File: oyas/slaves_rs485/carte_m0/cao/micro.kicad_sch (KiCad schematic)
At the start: 19 parts, among them J4 ISCP, U4 ATSAMD21G18A-A

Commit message: Finitions PCB
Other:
- company: (none) -> BPC
- title: (none) -> Carte Oya M0
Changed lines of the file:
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@@
 (kicad_sch (version 20230121) (generator eeschema)
   (paper "A4")
+  (title_block
+    (title "Carte Oya M0")
+    (date "2026-03-06")
+    (rev "Rev A")
+    (company "BPC")
+  )
   (junction (at 137.16 175.26) (diameter 0) (color 0 0 0 0)
   )

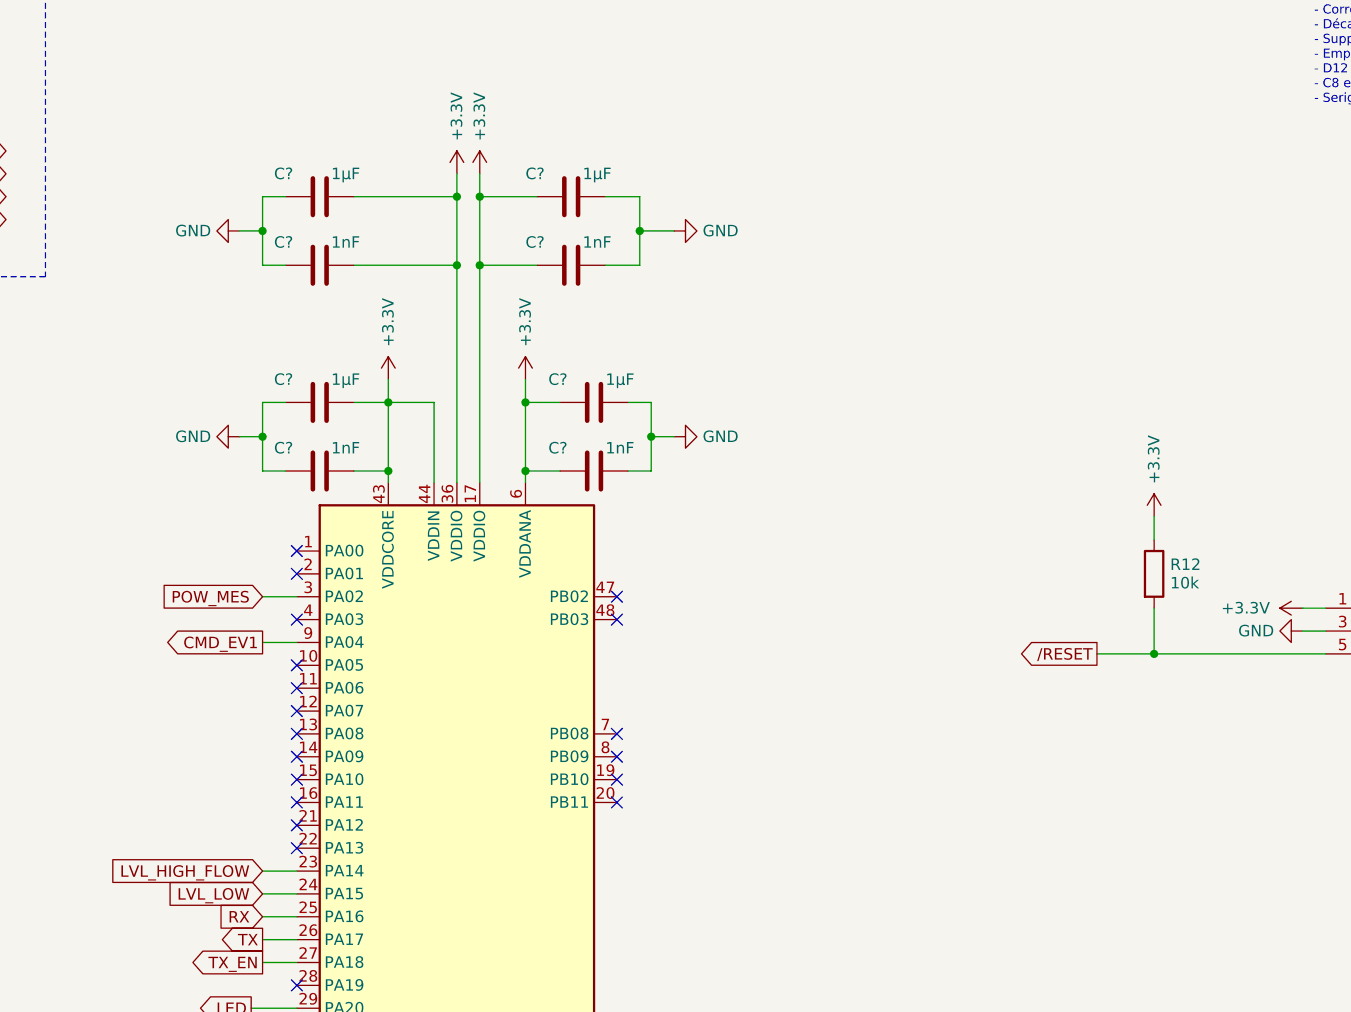
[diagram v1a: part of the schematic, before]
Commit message: Revue de carte et de routage:
- Amélioration découplage micro (1uF 805 sur VDDCore et 100nF 603 sur les autres selon recommendation microchip)
- R14=1k: Moins de courant dans Q1
- R1=R2=1k: Limiter le clamp en mode débit
- R3 NM en mode débit
- C17=100nF pour améliorer filtrage 3.3V
- Ajout Capa 100nF sur reset
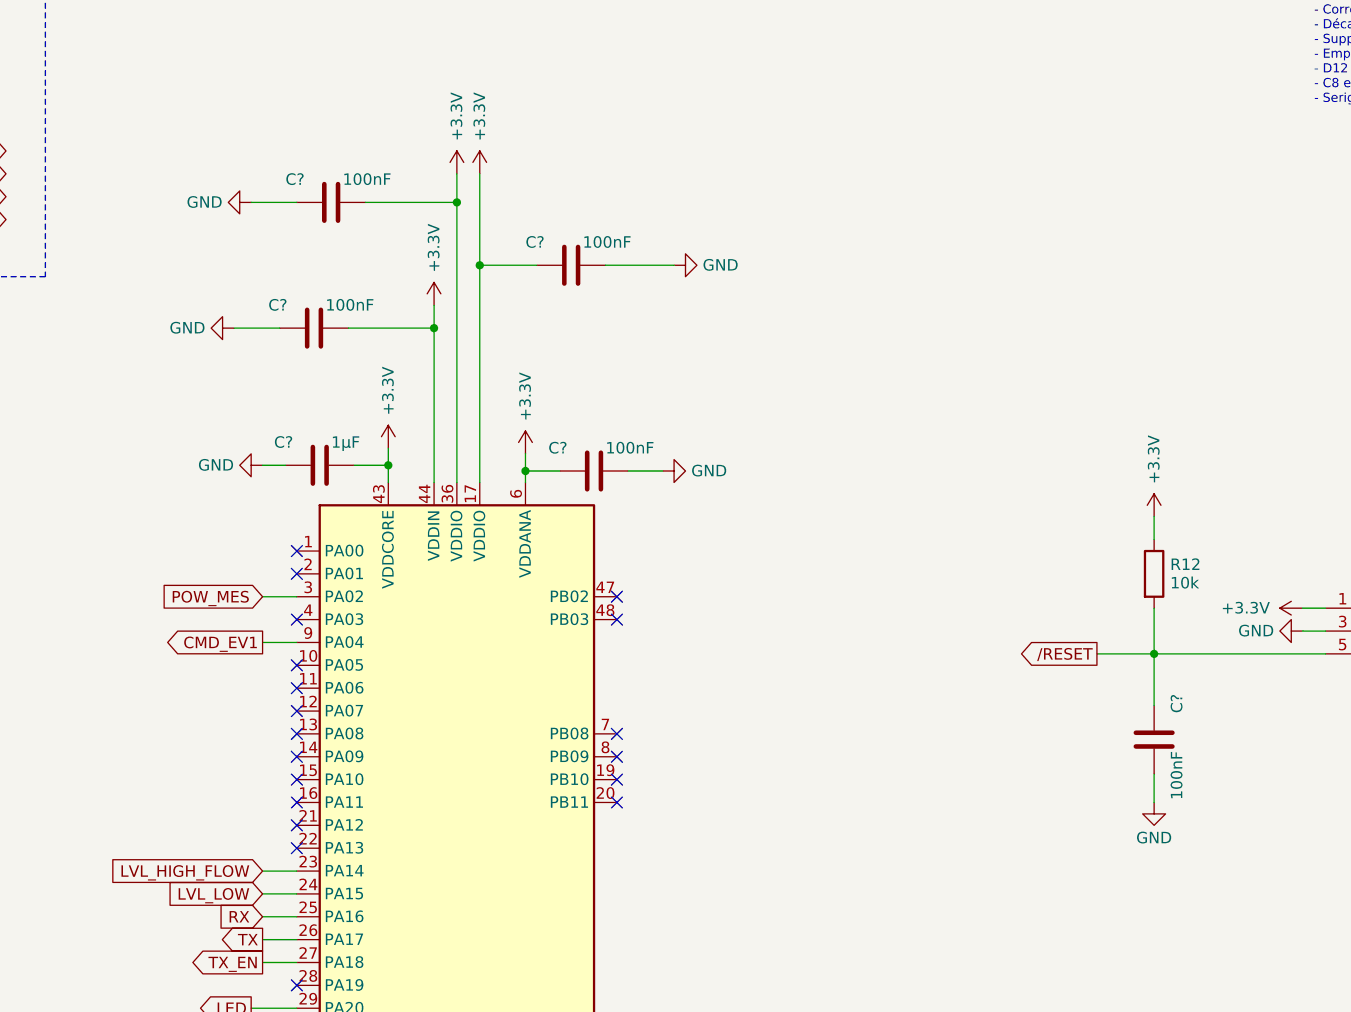
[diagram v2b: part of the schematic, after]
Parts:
- removed C? (x3): 1µF, Capacitor_SMD:C_0603_1608Metric_Pad1.08x0.95mm_HandSolder, symbol Device:C
- removed C?: 1nF, Capacitor_SMD:C_0603_1608Metric_Pad1.08x0.95mm_HandSolder, symbol Device:C
- added C?: 100nF, Capacitor_SMD:C_0603_1608Metric_Pad1.08x0.95mm_HandSolder, symbol Device:C
- added C?: 100nF, Capacitor_SMD:C_0805_2012Metric_Pad1.18x1.45mm_HandSolder, symbol Device:C
- C? (x3): value 1nF -> 100nF
- C?: footprint Capacitor_SMD:C_0603_1608Metric_Pad1.08x0.95mm_HandSolder -> Capacitor_SMD:C_0805_2012Metric_Pad1.18x1.45mm_HandSolder
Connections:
- net +3.3V: now also C?.1
- net GND: now also C?.1, C?.2
- net /RESET: now also C?.2
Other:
- moved on the sheet: C?

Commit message: Fin de revue avec ajout d'une diode TVS 18V en entrée
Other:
- title: Carte Oya M0 -> Esclave Oya M0
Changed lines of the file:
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@@
   (paper "A4")
   (title_block
-    (title "Carte Oya M0")
-    (date "2026-03-06")
-    (rev "Rev A")
+    (title "Esclave Oya M0")
+    (date "2026-03-07")
+    (rev "A")
     (company "BPC")
+    (comment 1 "Technologie avec M0 / Petite carte")
+    (comment 2 "Monitoring de tension d'alimentation")
+    (comment 3 "1 sortie 12V/5A - 2 entrées TOR (niveaux) ou 1 débimètre - 1 LED - RS485")
   )
   (junction (at 137.16 175.26) (diameter 0) (color 0 0 0 0)

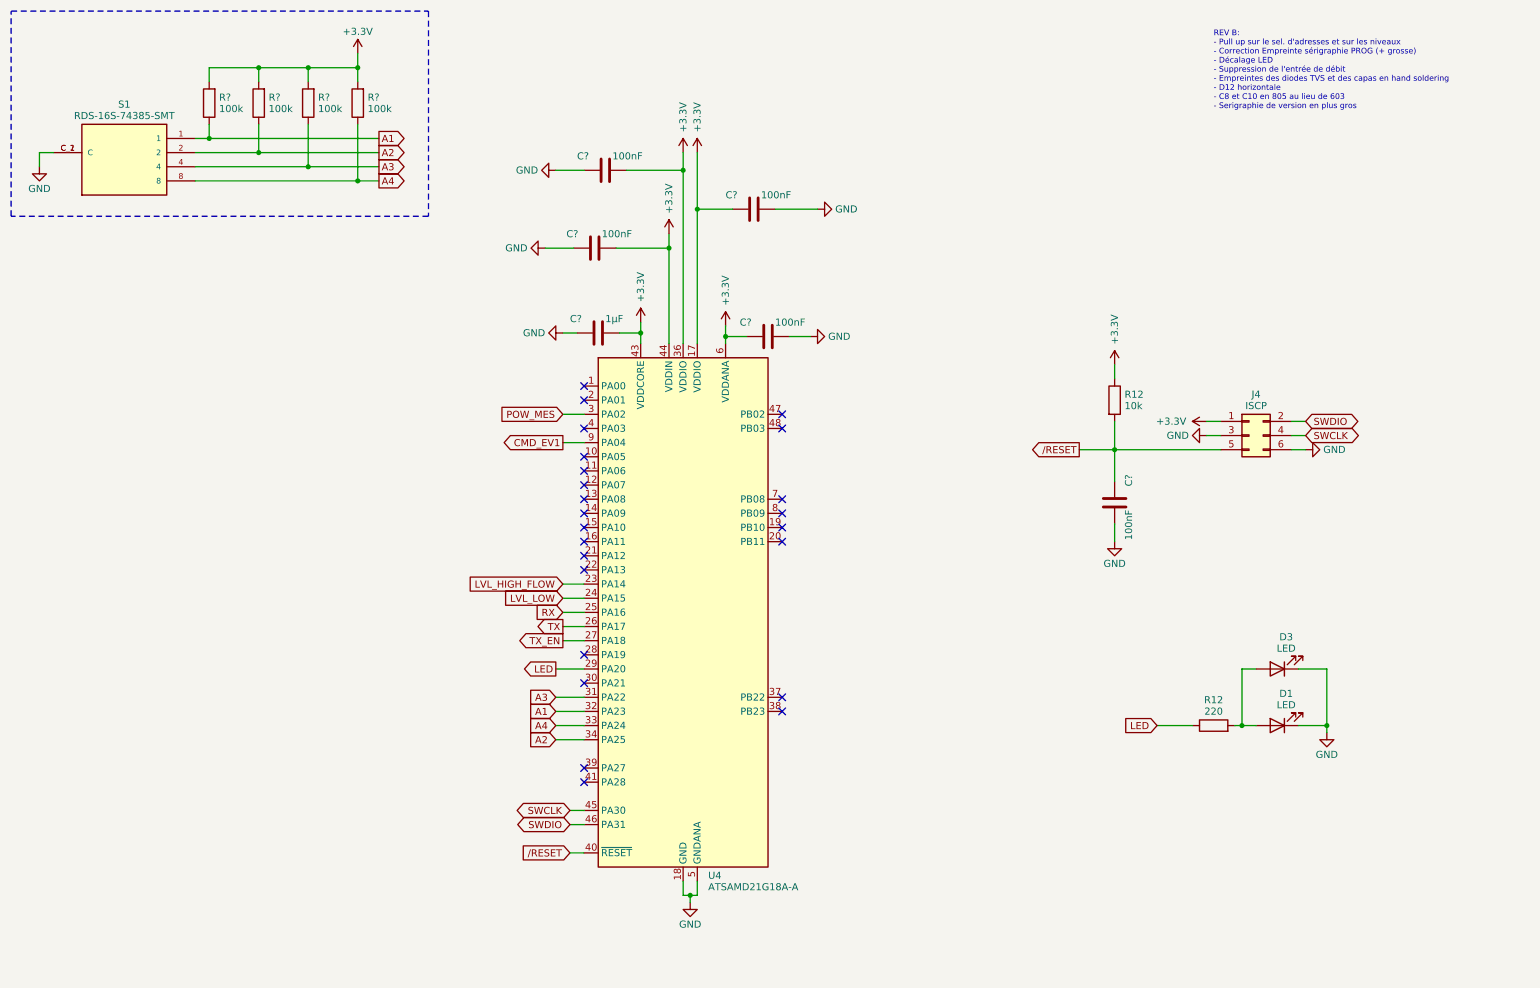
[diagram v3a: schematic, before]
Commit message: Préparation future carte Rev B (Inversion TX/RX) Programme en cours de test
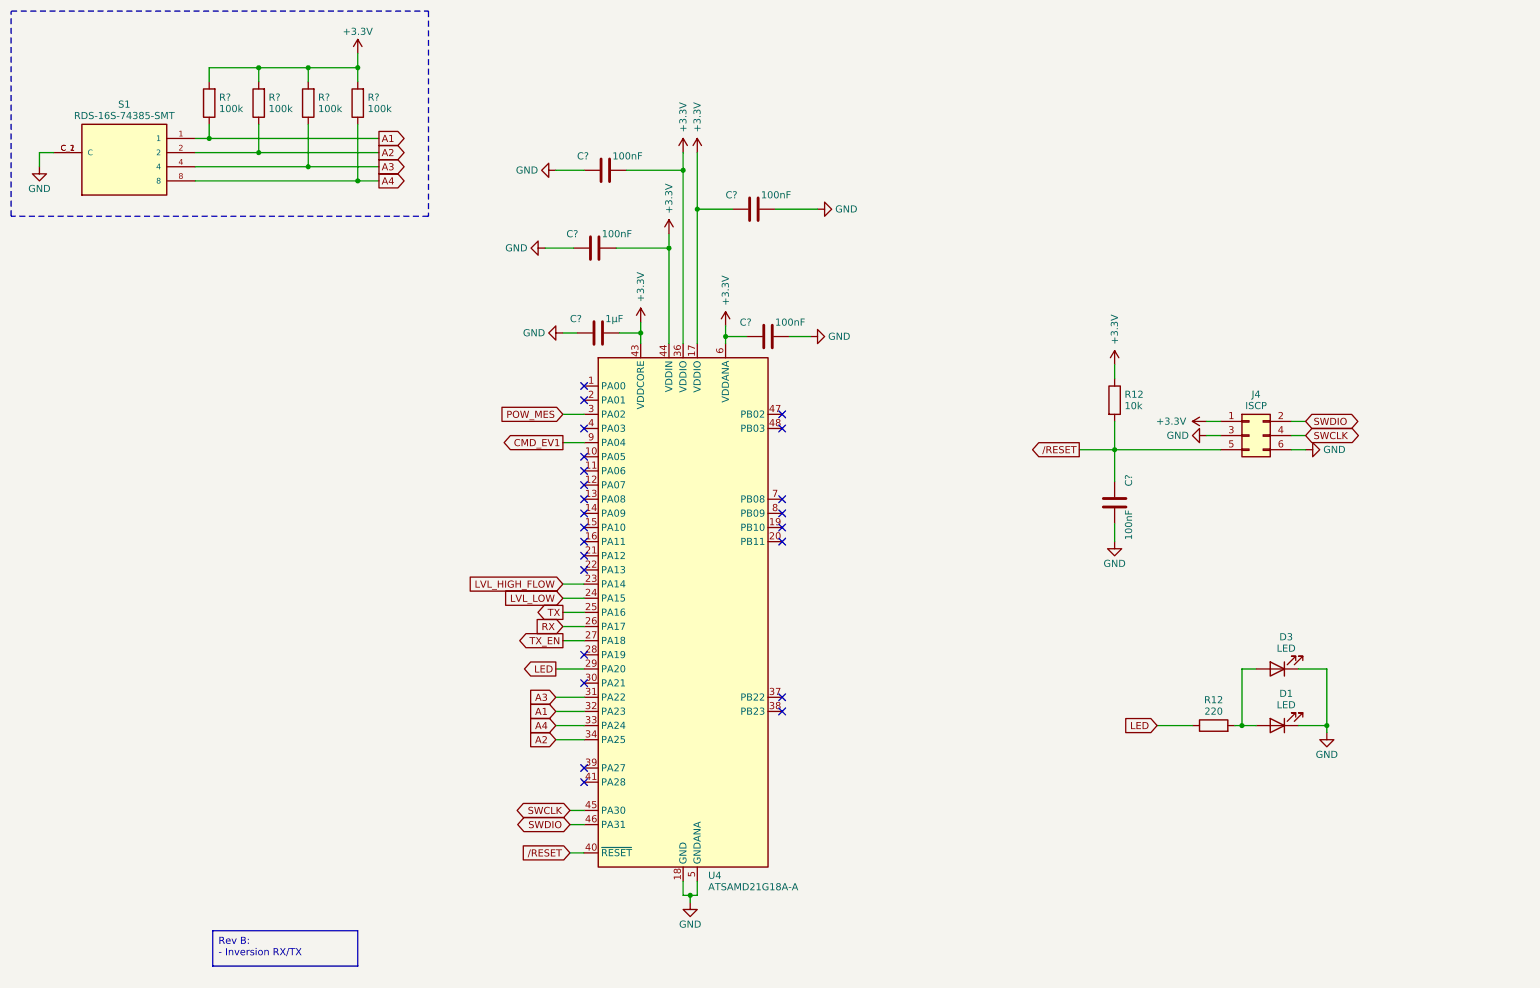
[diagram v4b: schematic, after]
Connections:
- net RX: now also U4.26 (PA17); no longer U4.25 (PA16)
- net TX: now also U4.25 (PA16); no longer U4.26 (PA17)
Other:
- note removed: "REV B: - Pull up sur le sel. d'adresses et sur les niveaux - Correction Empreinte sérigraphie PROG (+ grosse) - Décalage LED - Suppression de l'entrée de débit - Empreintes des diodes TVS et des capas en hand soldering - D12 horizontale - C8 et C10 en 805 au lieu de 603 - Serigraphie de version en plus gros"
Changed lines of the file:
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@@
   (title_block
     (title "Esclave Oya M0")
-    (date "2026-03-07")
-    (rev "A")
+    (date "2026-04-14")
+    (rev "B")
     (company "BPC")
     (comment 1 "Technologie avec M0 / Petite carte")
@@
     (fill (type none))
   )
-  (text "REV B:\n- Pull up sur le sel. d'adresses et sur les niveaux\n- Correction Empreinte sérigraphie PROG (+ grosse)\n- Décalage LED\n- Suppression de l'entrée de débit\n- Empreintes des diodes TVS et des capas en hand soldering\n- D12 horizontale\n- C8 et C10 en 805 au lieu de 603\n- Serigraphie de version en plus gros"
-    (at 231.14 34.29 0)
-    (effects (font (size 1.016 1.016)) (justify left bottom))
+  (text_box "Rev B:\n- Inversion RX/TX"
+    (at 51.435 181.61 0) (size 26.035 6.35)
+    (stroke (width 0) (type default))
+    (fill (type none))
+    (effects (font (size 1.27 1.27)) (justify left top))
   )
   (global_label "CMD_EV1" (shape output) (at 114.3 93.98 180) (fields_autoplaced)
@@
     )
   )
-  (global_label "TX" (shape output) (at 114.3 127 180) (fields_autoplaced)
-    (effects (font (size 1.27 1.27)) (justify right))
-    (property "Intersheetrefs" "${INTERSHEET_REFS}" (at 109.2171 127 0)
+  (global_label "TX" (shape output) (at 114.3 124.46 180) (fields_autoplaced)
+    (effects (font (size 1.27 1.27)) (justify right))
+    (property "Intersheetrefs" "${INTERSHEET_REFS}" (at 109.2171 124.46 0)
       (effects (font (size 1.27 1.27)) (justify right) hide)
     )
@@
     )
   )
-  (global_label "RX" (shape input) (at 114.3 124.46 180) (fields_autoplaced)
-    (effects (font (size 1.27 1.27)) (justify right))
-    (property "Intersheetrefs" "${INTERSHEET_REFS}" (at 108.9147 124.46 0)
-      (effects (font (size 1.27 1.27)) (justify right) hide)
-    )
+  (global_label "RX" (shape input) (at 114.3 127 180) (fields_autoplaced)
+    (effects (font (size 1.27 1.27)) (justify right))
+    (property "Intersheetrefs" "${INTERSHEET_REFS}" (at 108.9147 127 0)
+      (effects (font (size 1.27 1.27)) (justify right) hide)
+    )

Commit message: Changement connecteur de programmation
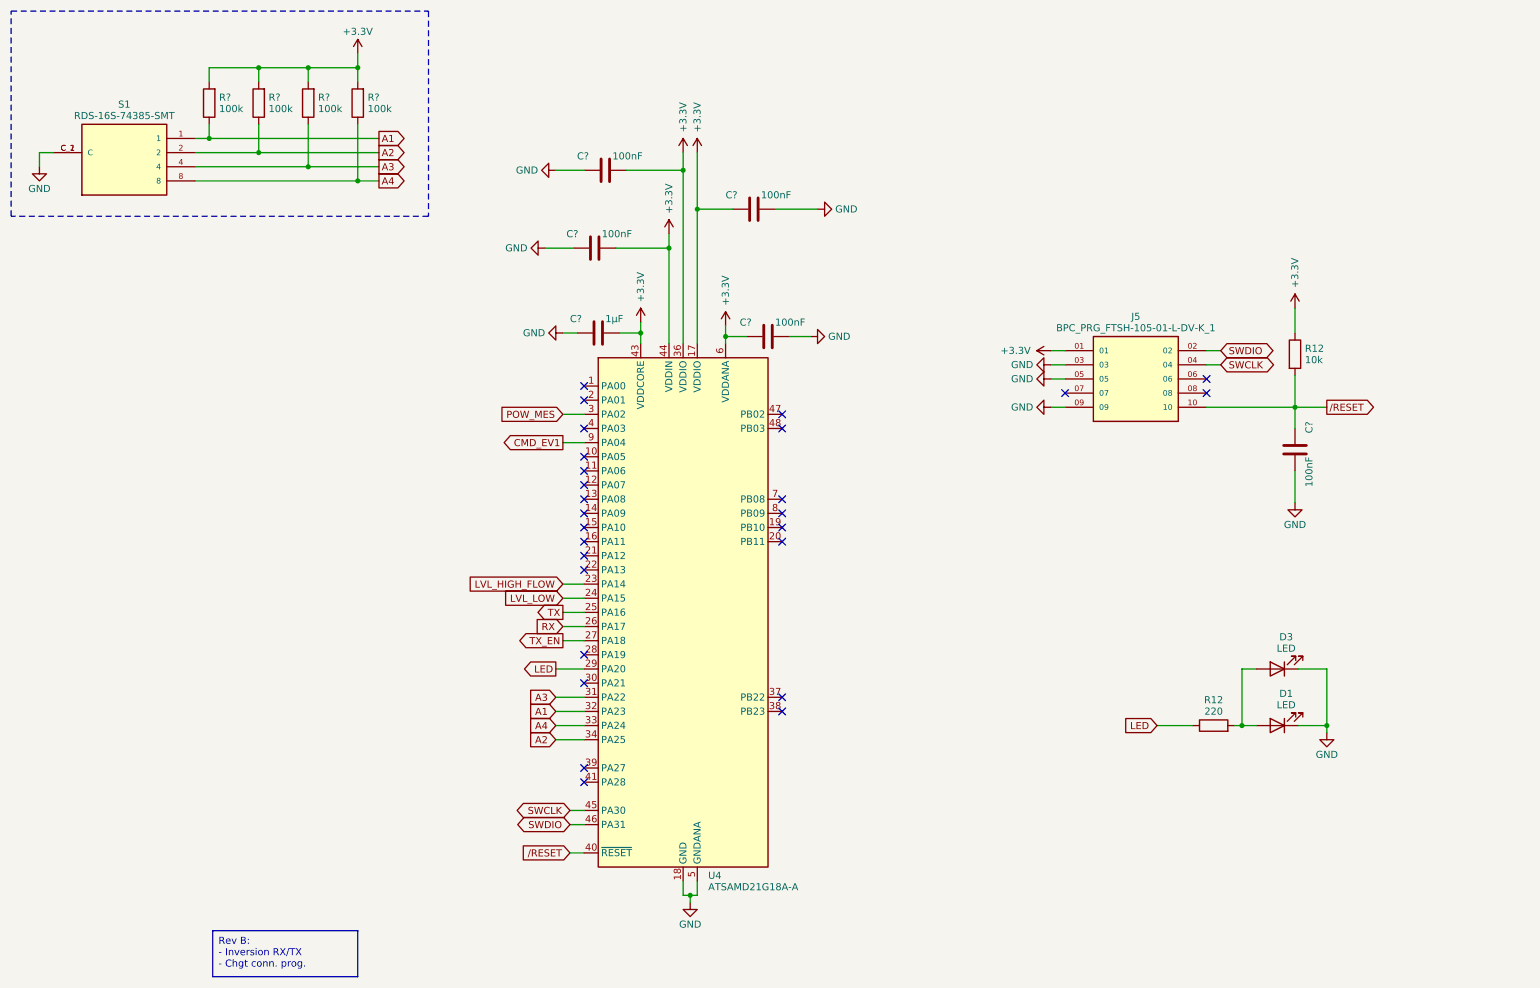
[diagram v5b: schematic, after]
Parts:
- removed J4: ISCP, bpc:BPC_ISCP_CMS, symbol bpc:BPC_ISCP
- added J5: BPC_PRG_FTSH-105-01-L-DV-K_1, bpc:BPC_SAMTEC_FTSH-105-01-L-DV-K, symbol bpc:BPC_PRG_FTSH-105-01-L-DV-K_1
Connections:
- net +3.3V: now also J5.01
- net GND: now also J5.03, J5.05, J5.09
- net SWCLK: now also J5.04
- net SWDIO: now also J5.02
- net /RESET: now also J5.10
- no-connect marks 24 -> 27
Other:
- moved on the sheet: C?, R12

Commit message: Finalisation Future Rev B
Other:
- title: Esclave Oya M0 -> Esclave Oya m0
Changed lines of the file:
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@@
   (paper "A4")
   (title_block
-    (title "Esclave Oya M0")
-    (date "2026-04-14")
+    (title "Esclave Oya m0")
+    (date "2026-05-13")
     (rev "B")
     (company "BPC")
@@
     (fill (type none))
   )
-  (text_box "Rev B:\n- Inversion RX/TX\n- Chgt conn. prog."
-    (at 51.435 181.61 0) (size 26.035 8.255)
-    (stroke (width 0) (type default))
-    (fill (type none))
-    (effects (font (size 1.27 1.27)) (justify left top))
-  )
   (global_label "CMD_EV1" (shape output) (at 114.3 93.98 180) (fields_autoplaced)
